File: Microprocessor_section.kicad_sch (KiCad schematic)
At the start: 18 parts, among them J9 Conn_01x04_Male, Q4 SS8050, Q5 SS8050, SW1 K2-1102SP-C4SC-04, U4 CH340C, U5 ESP32-WROOM-32D

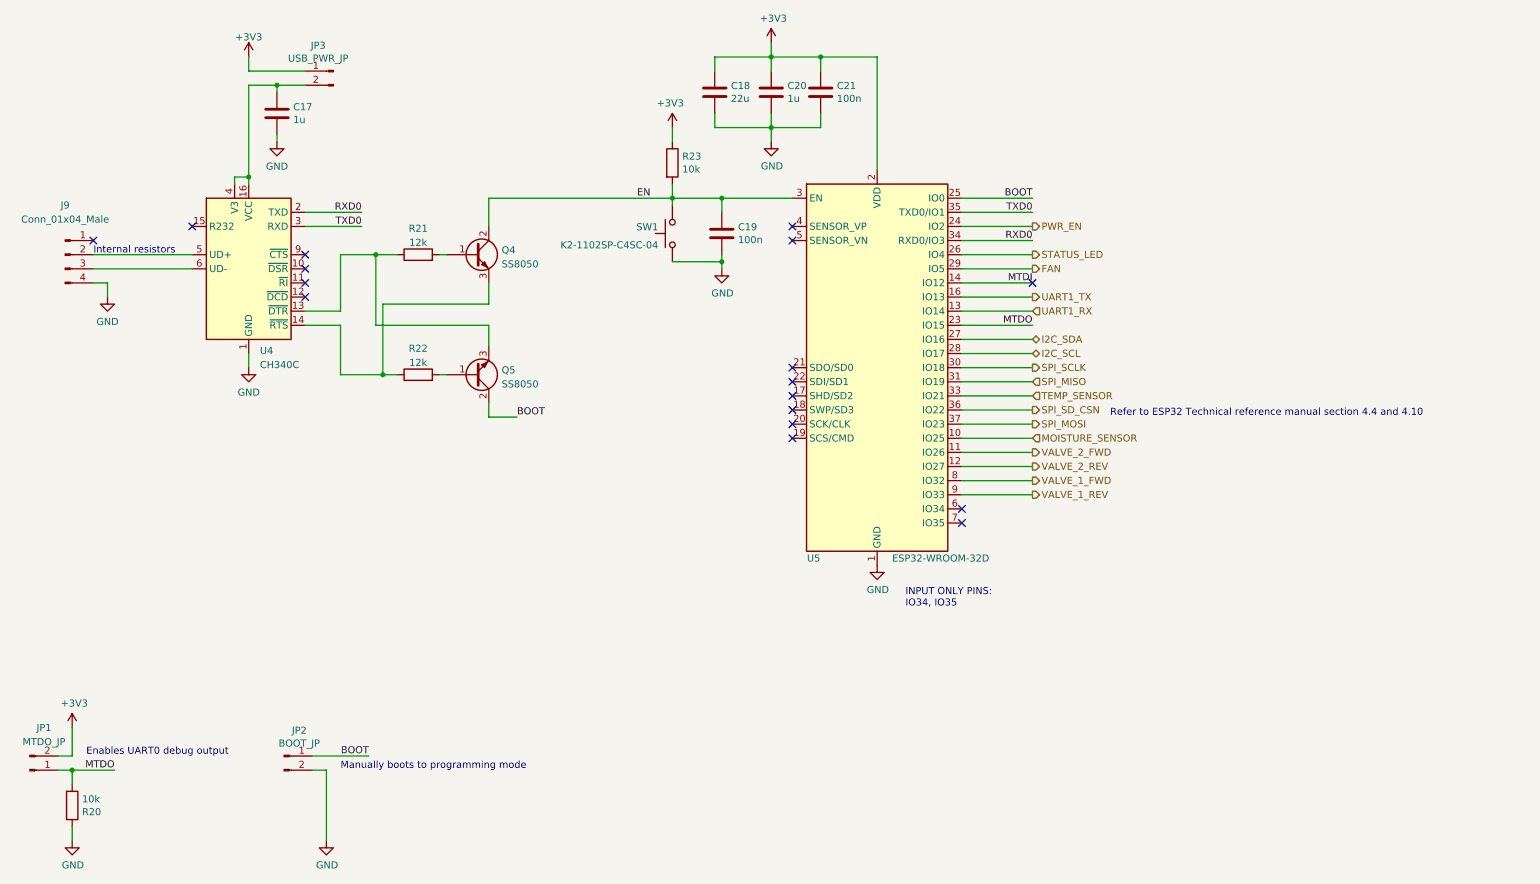
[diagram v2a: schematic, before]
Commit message: Finish routing round 2
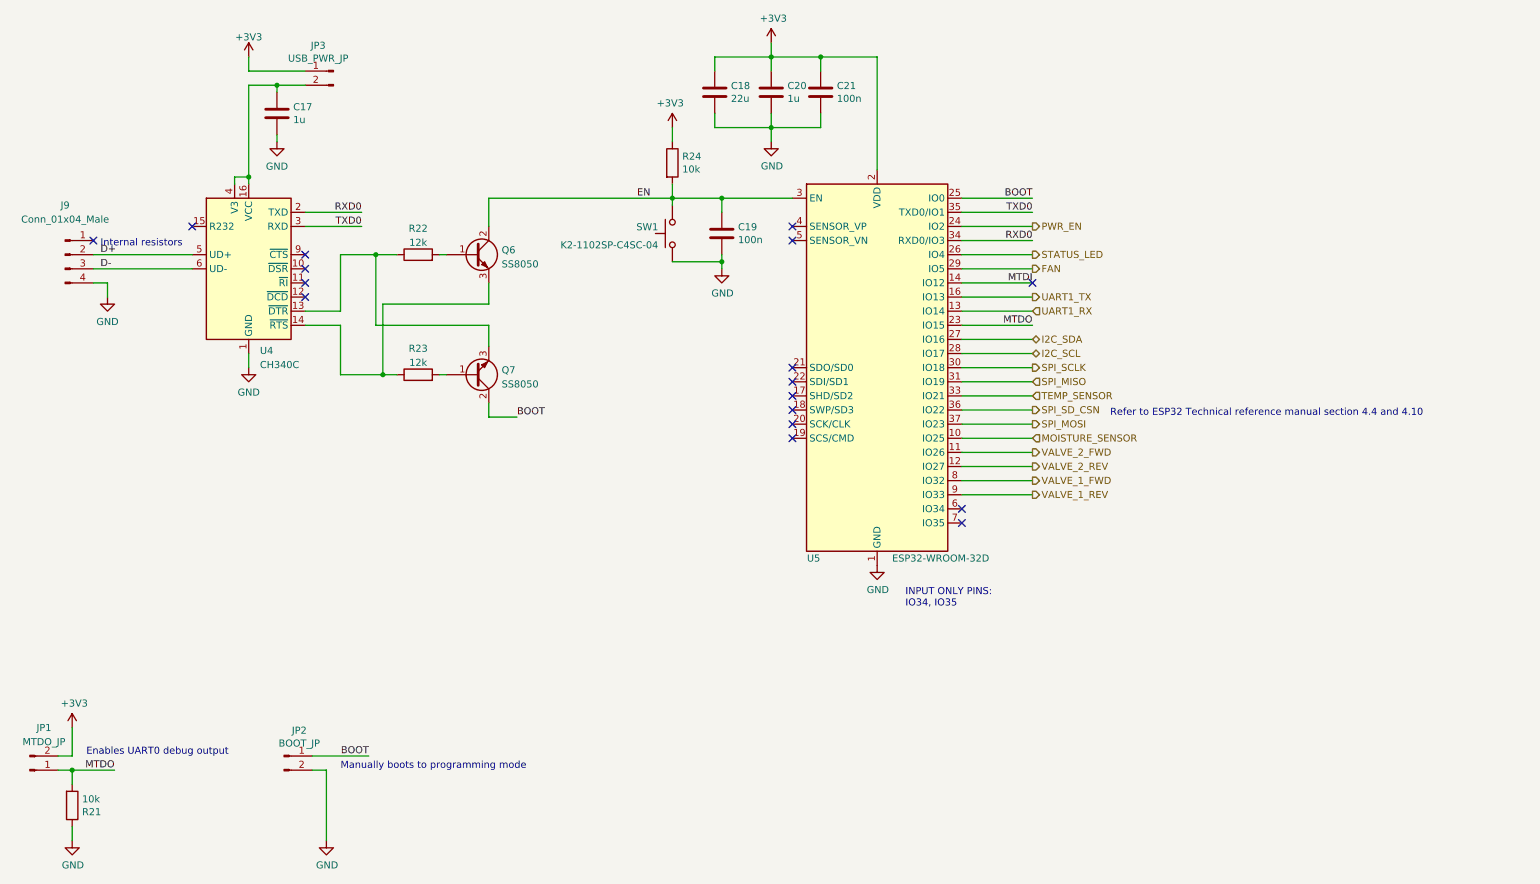
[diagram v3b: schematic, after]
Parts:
- renumbered Q4 to Q6, Q5 to Q7, R20 to R21, R21 to R22, R22 to R23, R23 to R24
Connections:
- net D+: now reaches J9.2 (Pin_2), U4.5 (UD+)
- net D-: now reaches J9.3 (Pin_3), U4.6 (UD-)
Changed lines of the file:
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@@
     (effects (font (size 1.27 1.27)) (justify left bottom))
   )
-  (text "Internal resistors\n" (at 36.83 81.28 0)
+  (text "Internal resistors\n" (at 38.1 80.01 0)
     (effects (font (size 1.27 1.27)) (justify left bottom))
   )
@@
     (effects (font (size 1.27 1.27)) (justify left bottom))
   )
+  (label "D+" (at 38.1 81.28 0)
+    (effects (font (size 1.27 1.27)) (justify left bottom))
+  )
   (label "TXD0" (at 85.09 76.2 180)
     (effects (font (size 1.27 1.27)) (justify right bottom))
@@
     (effects (font (size 1.27 1.27)) (justify right bottom))
   )
+  (label "D-" (at 38.1 83.82 0)
+    (effects (font (size 1.27 1.27)) (justify left bottom))
+  )
   (label "EN" (at 134.62 71.12 0)
     (effects (font (size 1.27 1.27)) (justify left bottom))
@@
   (symbol (lib_id "power:+3V3") (at 158.75 43.18 0) (unit 1)
     (in_bom yes) (on_board yes)
-    (property "Reference" "#PWR058" (id 0) (at 158.75 46.99 0)
+    (property "Reference" "#PWR060" (id 0) (at 158.75 46.99 0)
       (effects (font (size 1.27 1.27)) hide)
     )
@@
   (symbol (lib_id "power:+3V3") (at 140.97 58.42 0) (mirror y) (unit 1)
     (in_bom yes) (on_board yes)
-    (property "Reference" "#PWR056" (id 0) (at 140.97 62.23 0)
+    (property "Reference" "#PWR058" (id 0) (at 140.97 62.23 0)
       (effects (font (size 1.27 1.27)) hide)
     )
@@
   (symbol (lib_id "Device:R") (at 140.97 64.77 0) (unit 1)
     (in_bom yes) (on_board yes)
-    (property "Reference" "R23" (id 0) (at 142.748 63.6016 0)
+    (property "Reference" "R24" (id 0) (at 142.748 63.6016 0)
       (effects (font (size 1.27 1.27)) (justify left))
     )
@@
   (symbol (lib_id "power:GND") (at 158.75 60.96 0) (unit 1)
     (in_bom yes) (on_board yes)
-    (property "Reference" "#PWR059" (id 0) (at 158.75 67.31 0)
+    (property "Reference" "#PWR061" (id 0) (at 158.75 67.31 0)
       (effects (font (size 1.27 1.27)) hide)
     )
@@
   (symbol (lib_id "power:GND") (at 149.86 83.82 0) (unit 1)
     (in_bom yes) (on_board yes)
-    (property "Reference" "#PWR057" (id 0) (at 149.86 90.17 0)
+    (property "Reference" "#PWR059" (id 0) (at 149.86 90.17 0)
       (effects (font (size 1.27 1.27)) hide)
     )
@@
   (symbol (lib_id "power:+3V3") (at 33.02 166.37 0) (unit 1)
     (in_bom yes) (on_board yes)
-    (property "Reference" "#PWR048" (id 0) (at 33.02 170.18 0)
+    (property "Reference" "#PWR051" (id 0) (at 33.02 170.18 0)
       (effects (font (size 1.27 1.27)) hide)
     )
@@
   (symbol (lib_id "power:GND") (at 78.74 186.69 0) (unit 1)
     (in_bom yes) (on_board yes)
-    (property "Reference" "#PWR055" (id 0) (at 78.74 193.04 0)
+    (property "Reference" "#PWR057" (id 0) (at 78.74 193.04 0)
       (effects (font (size 1.27 1.27)) hide)
     )
@@
   (symbol (lib_id "Device:R") (at 33.02 180.34 0) (mirror x) (unit 1)
     (in_bom yes) (on_board yes)
-    (property "Reference" "R20" (id 0) (at 34.798 181.5084 0)
+    (property "Reference" "R21" (id 0) (at 34.798 181.5084 0)
       (effects (font (size 1.27 1.27)) (justify left))
     )
@@
   (symbol (lib_id "power:GND") (at 33.02 186.69 0) (unit 1)
     (in_bom yes) (on_board yes)
-    (property "Reference" "#PWR049" (id 0) (at 33.02 193.04 0)
+    (property "Reference" "#PWR052" (id 0) (at 33.02 193.04 0)
       (effects (font (size 1.27 1.27)) hide)
     )
@@
   (symbol (lib_id "power:GND") (at 177.8 137.16 0) (unit 1)
     (in_bom yes) (on_board yes)
-    (property "Reference" "#PWR060" (id 0) (at 177.8 143.51 0)
+    (property "Reference" "#PWR062" (id 0) (at 177.8 143.51 0)
       (effects (font (size 1.27 1.27)) hide)
     )
@@
   (symbol (lib_id "power:GND") (at 39.37 88.9 0) (unit 1)
     (in_bom yes) (on_board yes) (fields_autoplaced)
-    (property "Reference" "#PWR050" (id 0) (at 39.37 95.25 0)
+    (property "Reference" "#PWR053" (id 0) (at 39.37 95.25 0)
       (effects (font (size 1.27 1.27)) hide)
     )
@@
   (symbol (lib_id "Device:Q_NPN_BCE") (at 105.41 102.87 0) (mirror x) (unit 1)
     (in_bom yes) (on_board yes) (fields_autoplaced)
-    (property "Reference" "Q5" (id 0) (at 110.2614 102.0353 0)
+    (property "Reference" "Q7" (id 0) (at 110.2614 102.0353 0)
       (effects (font (size 1.27 1.27)) (justify left))
     )
@@
   (symbol (lib_id "power:GND") (at 64.77 101.6 0) (unit 1)
     (in_bom yes) (on_board yes) (fields_autoplaced)
-    (property "Reference" "#PWR054" (id 0) (at 64.77 107.95 0)
+    (property "Reference" "#PWR055" (id 0) (at 64.77 107.95 0)
       (effects (font (size 1.27 1.27)) hide)
     )
@@
   (symbol (lib_id "Device:Q_NPN_BCE") (at 105.41 81.28 0) (unit 1)
     (in_bom yes) (on_board yes) (fields_autoplaced)
-    (property "Reference" "Q4" (id 0) (at 110.2614 80.4453 0)
+    (property "Reference" "Q6" (id 0) (at 110.2614 80.4453 0)
       (effects (font (size 1.27 1.27)) (justify left))
     )
@@
   (symbol (lib_id "Device:R") (at 95.25 102.87 90) (unit 1)
     (in_bom yes) (on_board yes) (fields_autoplaced)
-    (property "Reference" "R22" (id 0) (at 95.25 98.1542 90))
+    (property "Reference" "R23" (id 0) (at 95.25 98.1542 90))
     (property "Value" "12k" (id 1) (at 95.25 100.6911 90))
     (property "Footprint" "Resistor_SMD:R_0603_1608Metric" (id 2) (at 95.25 104.648 90)
@@
   (symbol (lib_id "power:GND") (at 69.85 60.96 0) (unit 1)
     (in_bom yes) (on_board yes) (fields_autoplaced)
-    (property "Reference" "#PWR052" (id 0) (at 69.85 67.31 0)
+    (property "Reference" "#PWR056" (id 0) (at 69.85 67.31 0)
       (effects (font (size 1.27 1.27)) hide)
     )
@@
   (symbol (lib_id "Device:R") (at 95.25 81.28 90) (unit 1)
     (in_bom yes) (on_board yes) (fields_autoplaced)
-    (property "Reference" "R21" (id 0) (at 95.25 76.5642 90))
+    (property "Reference" "R22" (id 0) (at 95.25 76.5642 90))
     (property "Value" "12k" (id 1) (at 95.25 79.1011 90))
     (property "Footprint" "Resistor_SMD:R_0603_1608Metric" (id 2) (at 95.25 83.058 90)
@@
   (symbol (lib_id "power:+3V3") (at 64.77 45.72 0) (unit 1)
     (in_bom yes) (on_board yes)
-    (property "Reference" "#PWR053" (id 0) (at 64.77 49.53 0)
-      (effects (font (size 1.27 1.27)) hide)
-    )
+    (property "Reference" "#PWR054" (id 0) (at 64.77 49.53 0)
+      (effects (font (size 1.27 1.27)) hide)
+    )
